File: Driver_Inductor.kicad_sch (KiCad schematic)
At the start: 18 parts, among them J1 Control_A, J2 DC+, J3 DC-, J4 OUT1, J5 OUT2

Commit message: VER2_Test: сделал схему в один лист красиво
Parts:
- added C1, C2: 0.1u, Capacitor_SMD:C_0805_2012Metric_Pad1.18x1.45mm_HandSolder, symbol Device:C_Small
- added C11, C15, C16, C30, C31, C34, C35, C36, C9: 2.2u, Capacitor_SMD:C_0805_2012Metric_Pad1.18x1.45mm_HandSolder, symbol Device:C_Small
- added C17, C18, C23, C24, C25, C26: 10u, Capacitor_SMD:C_1210_3225Metric_Pad1.33x2.70mm_HandSolder, symbol Device:C
- added C20, C22: 10u, Capacitor_SMD:C_1210_3225Metric_Pad1.33x2.70mm_HandSolder, symbol Device:C_Small
- added C27: 4.7u, Capacitor_SMD:C_0805_2012Metric_Pad1.18x1.45mm_HandSolder, symbol Device:C_Small
- added C28: 1n, Capacitor_SMD:C_0805_2012Metric_Pad1.18x1.45mm_HandSolder, symbol Device:C_Small
- added C3, C33, C4, C7, C8: 56p, Capacitor_SMD:C_0805_2012Metric_Pad1.18x1.45mm_HandSolder, symbol Device:C_Small
- added C32: 10n, Capacitor_SMD:C_0805_2012Metric_Pad1.18x1.45mm_HandSolder, symbol Device:C_Small
- added C5, C6: 100p, Capacitor_SMD:C_0805_2012Metric_Pad1.18x1.45mm_HandSolder, symbol Device:C_Small
- added D1, D2: NSI6651ASC-DSWR, Package_SO:SOIC-16W_7.5x10.3mm_P1.27mm, symbol Driver_My:NSI6651
- added D10: RDY, LED_SMD:LED_0805_2012Metric_Pad1.15x1.40mm_HandSolder, symbol Device:LED_Small
- added D11, D8: WRA1215S-3WR2, Mornsun:WRA_S-3WR2, symbol Mornsun:WRA_S-3WR2
- added D12: K7805M-1000R3, Mornsun:K78xxM-1000R3, symbol Mornsun:K78xxM-1000R3 ÕýÊä³ö
- added D13, D15: SN65HVD3082EDR, Package_SO:SOIC-8_3.9x4.9mm_P1.27mm, symbol ADM1485JRZ:ADM1485JRZ
- added D14: SN65HVD3082EDR, Package_SO:SOIC-8_3.9x4.9mm_P1.27mm, symbol Interface_My:ADM3485E
- added D16, D18: 1SMB5919B, Diode_SMD:D_SOD-323_HandSoldering, symbol Device:D_Zener_Small
- added D17: NSM2011-50B5R-DSWR, Package_SO:SOIC-16W_7.5x10.3mm_P1.27mm, symbol Current_Sensor:NSM2011
- added D19: ADM3485E, Package_SO:SOIC-8_3.9x4.9mm_P1.27mm, symbol Interface_My:ADM3485E
- added D3, D4: MMSZ5240B, Diode_SMD:D_SOD-123, symbol Device:D_Schottky_Small
- added D5, D7: MURS160, Diode_SMD:D_SMA, symbol Device:D_Small
- added D6: SN74AHC1G08DBVR, Package_TO_SOT_SMD:SOT-23-5, symbol Logic_My:SN74AHC1G08DBVR
- added D9: FLT, LED_SMD:LED_0805_2012Metric_Pad1.15x1.40mm_HandSolder, symbol Device:LED_Small
- added Q1: BC817, Package_TO_SOT_SMD:SOT-23, symbol Transistor_FET:2N7002
- added R1, R2, R23, R29, R30, R31: 120, Resistor_SMD:R_0805_2012Metric_Pad1.20x1.40mm_HandSolder, symbol Device:R_Small
- added R11, R14, R32: 1k, Resistor_SMD:R_0805_2012Metric_Pad1.20x1.40mm_HandSolder, symbol Device:R_Small
- added R12, R35, R36, R37, R38: 560, Resistor_SMD:R_0805_2012Metric_Pad1.20x1.40mm_HandSolder, symbol Device:R_Small
- added R13, R25, R26, R27: 10k, Resistor_SMD:R_0805_2012Metric_Pad1.20x1.40mm_HandSolder, symbol Device:R_Small
- added R15, R16, R17, R18, R19, R20, R21, R22, R3, R4, R5, R6: 47, Resistor_SMD:R_1206_3216Metric_Pad1.30x1.75mm_HandSolder, symbol Device:R_Small
- added R24: 4.7k, Resistor_SMD:R_0805_2012Metric_Pad1.20x1.40mm_HandSolder, symbol Device:R_Small
- added R28: 2.2k, Resistor_SMD:R_0805_2012Metric_Pad1.20x1.40mm_HandSolder, symbol Device:R_Small
- added R7, R8: 1.6k, Resistor_SMD:R_0805_2012Metric_Pad1.20x1.40mm_HandSolder, symbol Device:R_Small
- added U3: LM1117GS-5.0, Package_TO_SOT_SMD:SOT-223, symbol Regulator_Linear:LM1117-3.3
- added U4: LMV7219M5, Package_TO_SOT_SMD:SOT-23-5, symbol Comparator:LMV7219M5
- added U5: SCM3728ASA, Package_SO:SOIC-8_3.9x4.9mm_P1.27mm, symbol Isolator:ADuM1200AR
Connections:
- net +15V: now also C17.1, C18.1, C20.1, D11.2 (Vin), D12.1 (Vin), D8.2 (Vin)
- net +VDC: now also D5.1 (K)
- net Current: now also C28.1, D17.12 (VOUT)
- net E2: now also C23.2, C24.1, C6.2, D1.3 (GND2), D4.2 (A), D8.7 (0V)
- net E3: now also C25.2, C26.1, C30.1, C5.2, D11.7 (0V), D2.3 (GND2), D3.2 (A), U3.3 (VI)
- net Fault_N: now also D14.7 (B), R23.1
- net Fault_P: now also D14.6 (A), R23.2
- net G2: now also D1.7 (CLAMP), R15.1, R16.1, R17.1, R18.1, R3.1, R4.1
- net G3: now also D2.7 (CLAMP), R19.1, R20.1, R21.1, R22.1, R5.1, R6.1
- net GND: now also C1.1, C11.2, C15.2, C16.2, C17.2, C18.2, C2.1, C20.2, C22.2, C27.2, C28.2, C3.1, C35.2, C36.2, C4.1, C7.2, C8.2, C9.2, D1.11 (IN-), D1.16 (TEST), D1.9 (GND1), D10.1 (K), D11.1 (GND), D12.2 (GND), D13.2 (~{RE}), D13.3 (DE), D13.5 (GND), D14.5 (GND), D15.2 (~{RE}), D15.3 (DE), D15.5 (GND), D17.15 (GND), D19.5 (GND), D2.11 (IN-), D2.16 (TEST), D2.9 (GND1), D6.3 (GND), D8.1 (GND), Q1.2 (S), R36.2, R38.2, U5.5 (GND2)
- net NTC1: now also C32.1, U4.4 (-)
- net NTC2: now also R28.2
- net OUT1: now also D7.1 (K)
- net OUT2: now also D17.5 (IP-), D17.6 (IP-), D17.7 (IP-), D17.8 (IP-)
- net OUT2_Sens: now also D17.1 (IP+), D17.2 (IP+), D17.3 (IP+), D17.4 (IP+)
- net PWM1_N: now also D15.7 (B), R30.1, R37.2
- net PWM1_P: now also D15.6 (A), R30.2, R38.1
- net PWM2_N: now also D13.7 (B), R31.1, R35.2
- net PWM2_P: now also D13.6 (A), R31.2, R36.1
- net Reset: now also R24.1
- net Temp_N: now also D19.7 (B), R29.1
- net Temp_P: now also D19.6 (A), R29.2
- new net: D2.4 (OUTH), R20.2, R21.2, R22.2
- new net: C5.1, D2.2 (DESAT), D3.1 (K), R8.2
- new net: D1.6 (OUTL), R15.2, R16.2, R3.2
- new net: D16.2 (A), D5.2 (A)
- new net: Q1.1 (G), R24.2
- new net: D10.2 (A), R12.1
- new net: C33.2, R27.2, R28.1, U4.1, U5.2 (VIA)
- new net: D19.4 (DI), U5.7 (VOA)
- new net: D2.6 (OUTL), R19.2, R5.2, R6.2
- new net: C33.1, R25.1, R26.2, R27.1, U4.3 (+)
- new net: D15.1 (RO), D2.10 (IN+)
- new net: C4.2, D2.14 (~{RST}), R2.2
- new net: C3.2, D1.14 (~{RST}), R1.2
- new net: D1.10 (IN+), D13.1 (RO)
- new net: C6.1, D1.2 (DESAT), D4.1 (K), R7.2
- new net: D16.1 (K), R8.1
- new net: D1.4 (OUTH), R17.2, R18.2, R4.2
- new net: D14.4 (DI), D6.4 (Y)
- new net: D18.1 (K), R7.1
- new net: D18.2 (A), D7.2 (A)
- new net: D9.2 (A), R11.1
- new net +15V_H: C26.2, D11.6 (+VO), D2.5 (Vcc2)
- new net +15V_L: C24.2, D1.5 (Vcc2), D8.6 (+VO)
- new net +5V: C1.2, C11.1, C15.1, C16.1, C2.2, C22.1, C27.1, C35.1, C36.1, C9.1, D1.15 (Vcc1), D12.3 (+Vo), D13.8 (VCC), D14.2 (RE), D14.3 (DE), D14.8 (VCC), D15.8 (VCC), D17.10 (VCC), D19.2 (RE), D19.3 (DE), D19.8 (VCC), D2.15 (Vcc1), D6.5 (Vcc), R11.2, R13.2, R14.2, R32.2, R35.1, R37.1, U5.8 (VDD2)
- new net +5VP: C31.1, C34.1, R25.2, U3.2 (VO), U4.5 (V+), U5.1 (VDD1)
- new net -15V_H: C25.1, C30.2, C31.2, C32.2, C34.2, D11.8 (-Vo), D2.1 (Vee2), D2.8 (Vee2), R26.1, U3.1 (GND), U4.2 (V-), U5.4 (GND1)
- new net -15V_L: C23.1, D1.1 (Vee2), D1.8 (Vee2), D8.8 (-Vo)
- new net FLT: C7.1, D1.13 (~{FLT}), D2.13 (~{FLT}), D6.2 (A), D9.1 (K), R13.1
- new net RDY: C8.1, D1.12 (RDY), D2.12 (RDY), D6.1 (B), R12.2, R14.1
- new net RST: Q1.3 (D), R1.1, R2.1, R32.1
- no-connect marks 6 -> 17
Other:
- removed sheet Current_Sensor
- removed sheet Driver
- removed sheet Indication
- removed sheet NTC
- removed sheet Power_Supply
- removed sheet Reset
- note added: "Desat Level 2.0V"
- note added: "Датчик тока"
- note added: "Драйвер верхнего ключа"
- note added: "Драйвер нижнего ключа"
- note added: "Ошибка драйверо"
- note added: "Питание +5В"
- note added: "Питание драйверов"
- note added: "Преобразование температуры IGBT"
- note added: "Сброс ошибки драйвера"
- note added: "Трехфазный модуль"
- note added: "Управляющий разъем"
- moved on the sheet: C10, C12, C13, C14, C19, C21, C29, C37, D20, J1, J2, J3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

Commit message: VER2_Test: добавил СБ и 3D модели
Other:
- note added: "НВЦТ.EVP150-2-1.2000.220"
- note added: "Схема электрическая принципиальная"
- company: (none) -> ООО "Электротранспортные технологии"
- title: (none) -> Плата драйверов модуля обмотки возбуждения
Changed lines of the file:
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@@
 	(generator_version "9.0")
 	(paper "A2")
+	(title_block
+		(title "Плата драйверов модуля обмотки возбуждения")
+		(company "ООО \"Электротранспортные технологии\"")
+		(comment 1 "НВЦТ.EVP150-2-1.2000.220 Э3")
+		(comment 2 "Филатов А.С.")
+		(comment 3 "Сизякин А.В.")
+		(comment 4 "Коваленко В.А.")
+		(comment 6 "Зубков Д.Н.")
+	)
 	(rectangle
 		(start 82.677 225.425)
@@
 		)
 	)
+	(text "Схема электрическая принципиальная"
+		(exclude_from_sim no)
+		(at 503.682 394.97 0)
+		(effects
+			(font
+				(size 2.5 2.5)
+			)
+		)
+	)
 	(text "Датчик тока "
 		(exclude_from_sim no)
@@
 			)
 		)
+	)
+	(text "НВЦТ.EVP150-2-1.2000.220"
+		(exclude_from_sim no)
+		(at 16.51 159.004 90)
+		(effects
+			(font
+				(size 2.5 2.5)
+			)
+		)

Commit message: VER2_Test: исправил Э3
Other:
- note added: "1. Перечень элементтов см. НВЦТ.EVP150-2-1.2000.220 ПЭ3."
- note added: "ООО "Электротранспортные"
- note added: "технологии""
- company: ООО "Электротранспортные технологии" -> (none)
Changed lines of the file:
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@@
 	(title_block
 		(title "Плата драйверов модуля обмотки возбуждения")
-		(company "ООО \"Электротранспортные технологии\"")
 		(comment 1 "НВЦТ.EVP150-2-1.2000.220 Э3")
 		(comment 2 "Филатов А.С.")
@@
 		)
 	)
+	(text "технологии\""
+		(exclude_from_sim no)
+		(at 563.88 409.702 0)
+		(effects
+			(font
+				(size 2.5 2.5)
+			)
+		)
+	)
 	(text "Схема электрическая принципиальная"
 		(exclude_from_sim no)
@@
 		)
 	)
+	(text "ООО \"Электротранспортные"
+		(exclude_from_sim no)
+		(at 563.88 405.892 0)
+		(effects
+			(font
+				(size 2.5 2.5)
+			)
+		)
+	)
 	(text "Ошибка драйверо"
 		(exclude_from_sim no)
@@
 		(effects
 			(font
+				(size 3.5 3.5)
+			)
+		)
+	)
+	(text "1. Перечень элементтов см. НВЦТ.EVP150-2-1.2000.220 ПЭ3."
+		(exclude_from_sim no)
+		(at 467.36 339.598 0)
+		(effects
+			(font

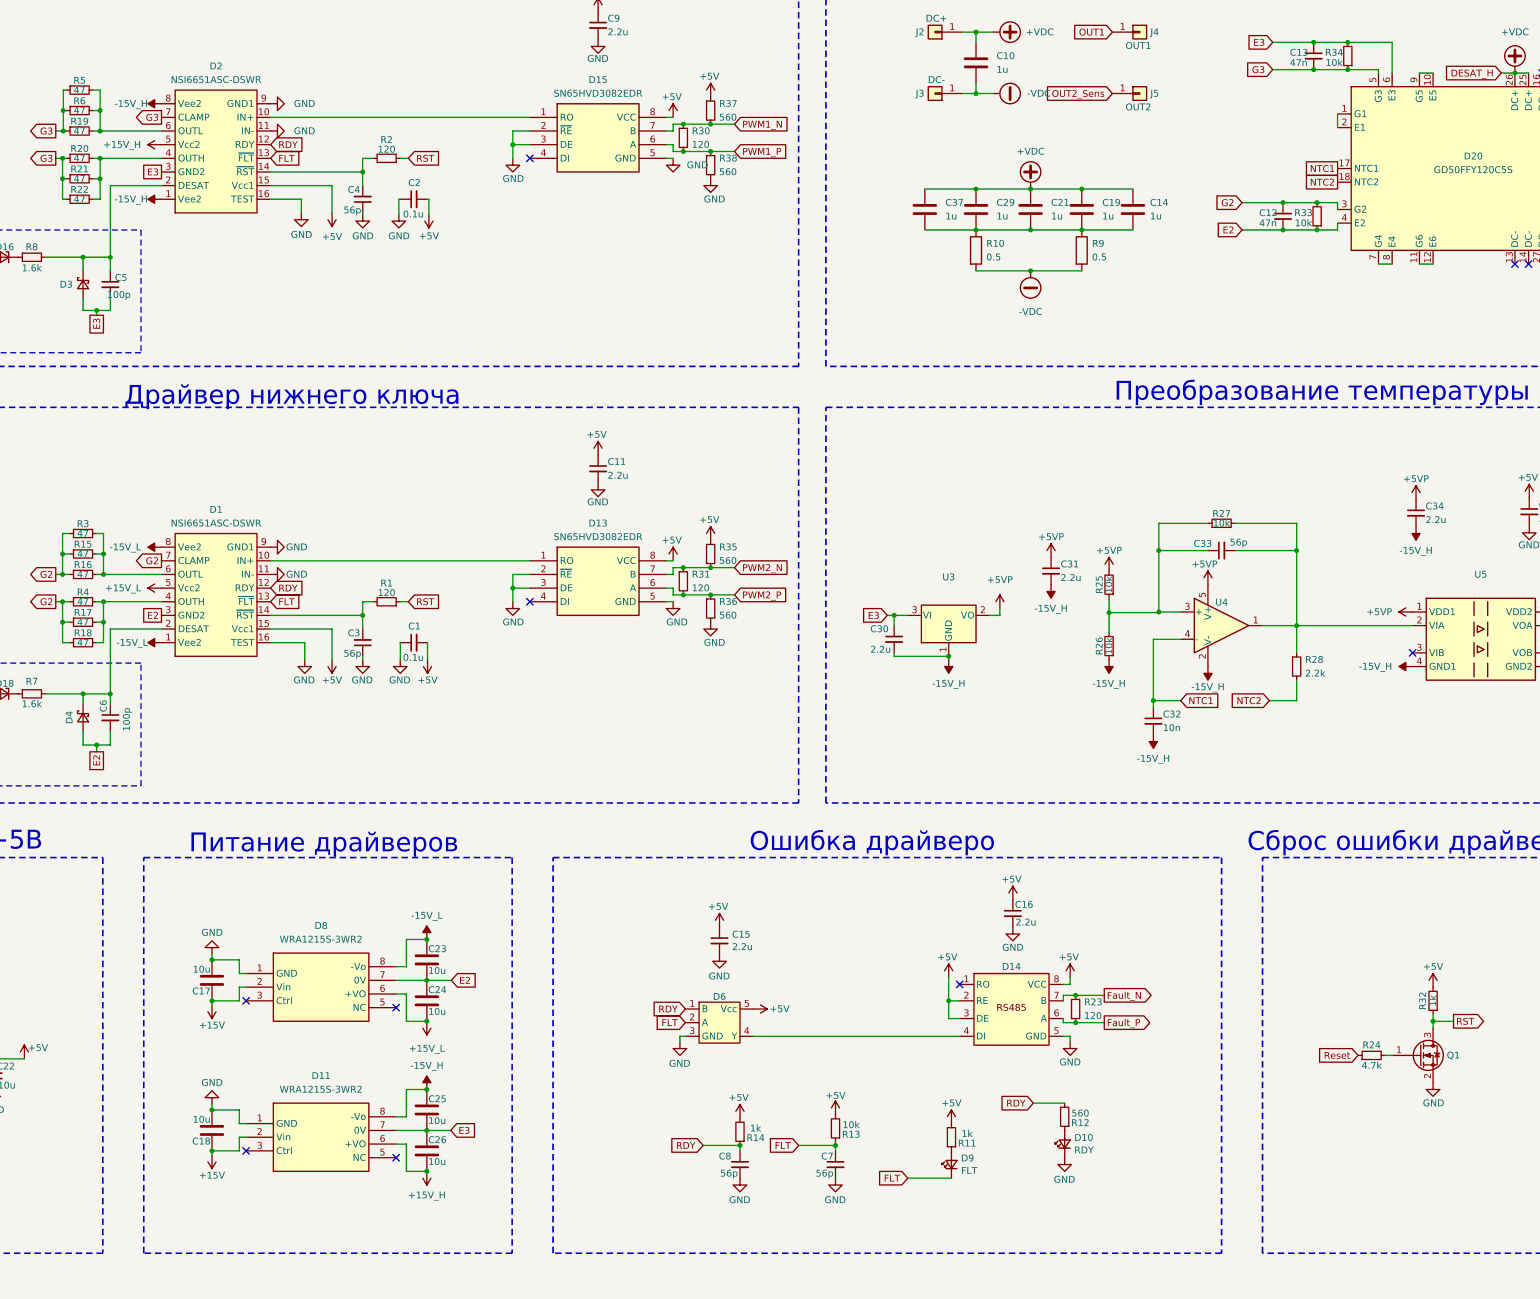
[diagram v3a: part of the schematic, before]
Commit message: VER2_Test: заменил источники на QA1
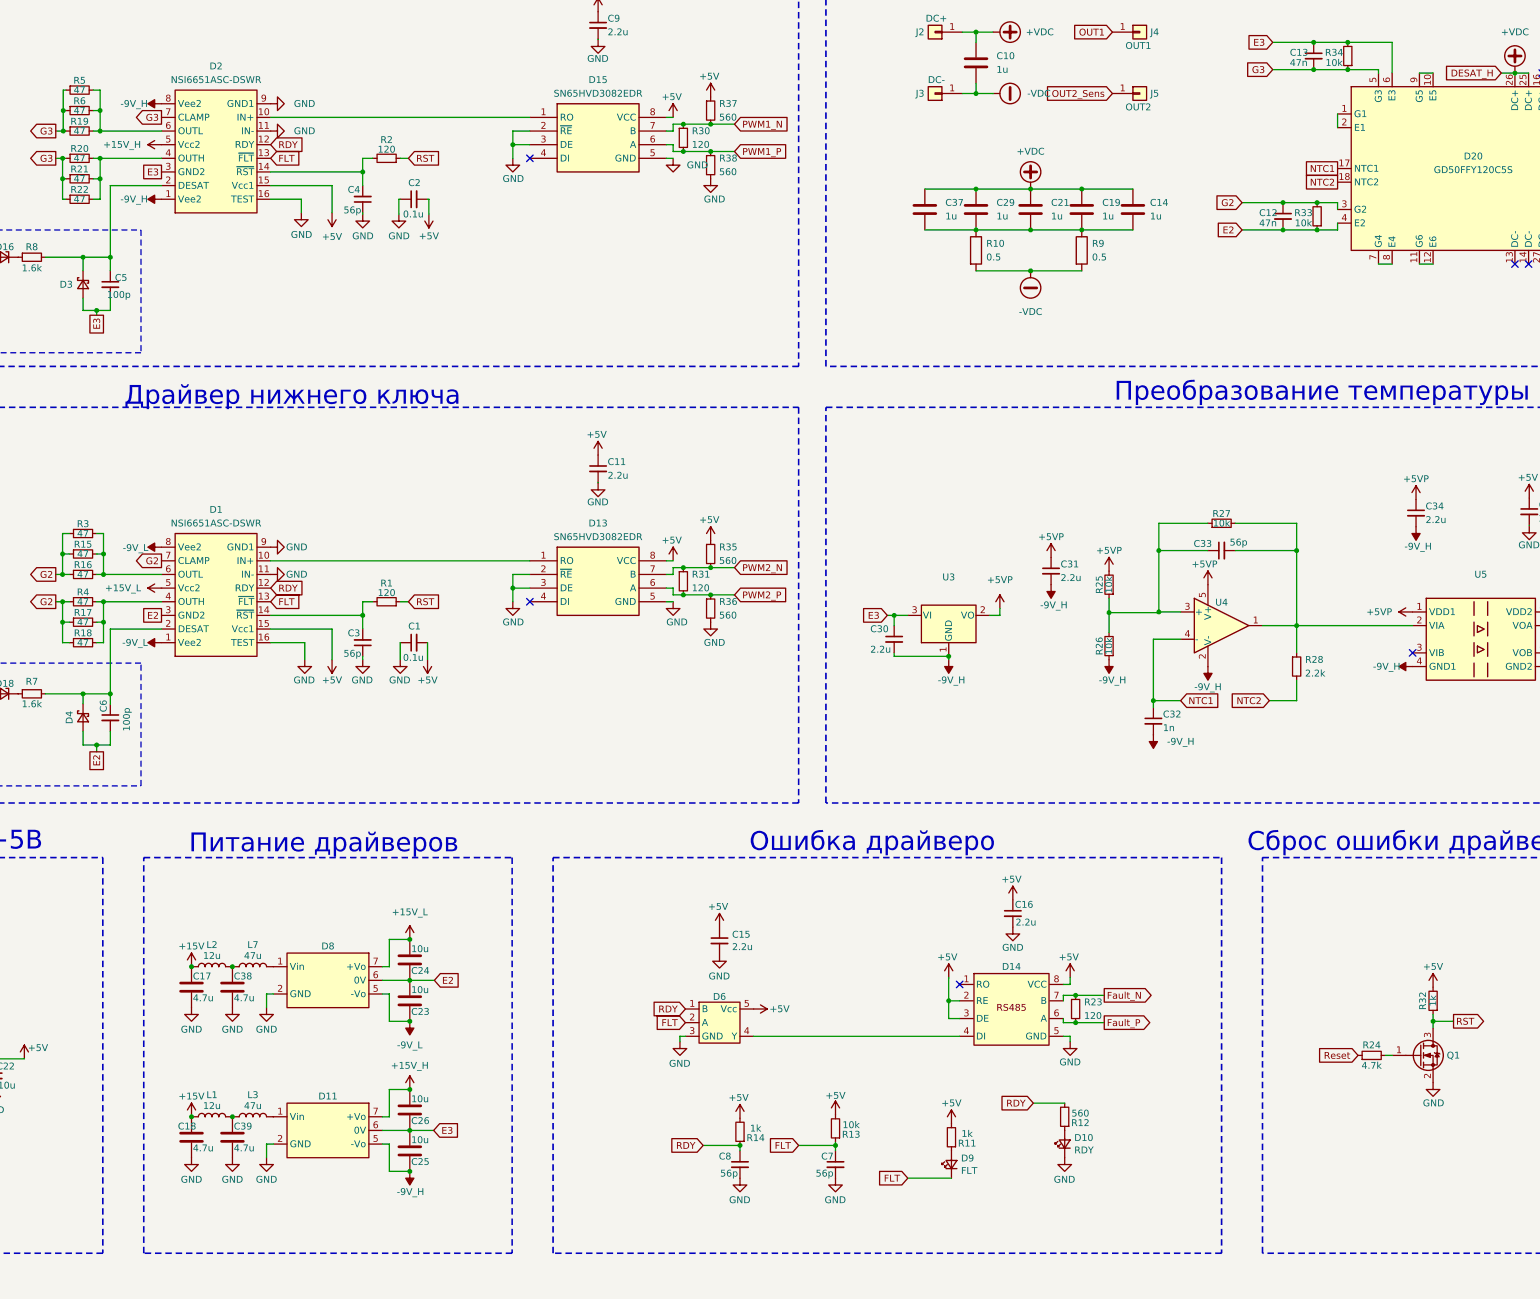
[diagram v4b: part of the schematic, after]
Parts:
- removed D11, D8: WRA1215S-3WR2, Mornsun:WRA_S-3WR2, symbol Mornsun:WRA_S-3WR2
- added C38, C39: 4.7u, Capacitor_SMD:C_1206_3216Metric_Pad1.33x1.80mm_HandSolder, symbol Device:C
- added D11, D8: ~, Mornsun:QA, symbol Mornsun:QA
- added L1, L2: 12u, Inductor_SMD:L_1210_3225Metric_Pad1.42x2.65mm_HandSolder, symbol Device:L
- added L3, L7: 47u, Inductor_SMD:L_1812_4532Metric_Pad1.30x3.40mm_HandSolder, symbol Device:L
- C17, C18: value 10u -> 4.7u; footprint Capacitor_SMD:C_1210_3225Metric_Pad1.33x2.70mm_HandSolder -> Capacitor_SMD:C_1206_3216Metric_Pad1.33x1.80mm_HandSolder
- C32: value 10n -> 1n
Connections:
- net +15V: now also L1.1, L2.1
- net +15V_H: now also D11.7 (+Vo)
- net +15V_L: now also D8.7 (+Vo)
- net E2: now also D8.6 (0V)
- net E3: now also D11.6 (0V)
- net GND: now also C38.2, C39.2, D11.2 (GND), D8.2 (GND)
- net -15V_H renamed -9V_H
- net -9V_H: now also D11.5 (-Vo)
- net -15V_L renamed -9V_L
- net -9V_L: now also D8.5 (-Vo)
- new net: C39.1, L1.2, L3.1
- new net: D11.1 (Vin), L3.2
- new net: C38.1, L2.2, L7.1
- new net: D8.1 (Vin), L7.2
- no-connect marks 17 -> 13
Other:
- moved on the sheet: C17, C18, C23, C24, C25, C26

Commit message: VER2.3: оптимизировал трассировку + сделал BOM
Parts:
- removed R18, R22, R3, R5: 47, Resistor_SMD:R_1206_3216Metric_Pad1.30x1.75mm_HandSolder, symbol Device:R_Small
- C23, C24, C25, C26: footprint Capacitor_SMD:C_1210_3225Metric_Pad1.33x2.70mm_HandSolder -> Capacitor_SMD:C_1206_3216Metric_Pad1.33x1.80mm_HandSolder
- D1, D2: value NSI6651ASC-DSWR -> ~; Product Name (none) -> NSI6651ASC-DSWR
- D10: value RDY -> ~; Product Name (none) -> FYLS-0805UBC; Purpose (none) -> RDY
- D12: value K7805M-1000R3 -> ~; Product Name (none) -> K7805M-1000R3
- D13, D14, D15: value SN65HVD3082EDR -> ~; Product Name (none) -> SN65HVD3082EDR
- D16, D18: value 1SMB5919B -> ~; Product Name (none) -> 1SMB5919B
- D17: value NSM2011-50B5R-DSWR -> ~; Product Name (none) -> NSM2011-50B5R-DSWR
- D19: value ADM3485E -> ~; Product Name (none) -> SN65HVD3082EDR
- D3, D4: value MMSZ5240B -> ~; Product Name (none) -> MMSZ5240B
- D5, D7: value MURS160 -> ~; Product Name (none) -> MURS160
- D6: value SN74AHC1G08DBVR -> ~; Product Name (none) -> SN74AHC1G08DBVR
- D9: value FLT -> ~; Product Name (none) -> FYLS-0805URC; Purpose (none) -> FLT
- J1: value Control_A -> ~; Product Name (none) -> SCT3001WV-2x06P; Purpose (none) -> Control_A
- J2: value DC+ -> ~; Purpose (none) -> DC+
- J3: value DC- -> ~; Purpose (none) -> DC-
- J4: value OUT1 -> ~; Purpose (none) -> OUT1
- J5: value OUT2 -> ~; Purpose (none) -> OUT2
- Q1: value BC817 -> ~; Product Name (none) -> BC817
- R15, R16, R17, R4: value 47 -> 30
- U3: value LM1117GS-5.0 -> ~; Product Name (none) -> LM1117GS-5.0
- U4: value LMV7219M5 -> ~; Product Name (none) -> LMV7219M5
- U5: value SCM3728ASA -> ~; Product Name (none) -> SCM3728ASA
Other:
- note added: "1. Перечень элементтов см. НВЦТ.EVP150-2-1.2000.220 ПЭ3_v2.3."
- note removed: "1. Перечень элементтов см. НВЦТ.EVP150-2-1.2000.220 ПЭ3."
